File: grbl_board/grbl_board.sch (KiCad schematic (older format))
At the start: 6 parts, among them J1 COOL, J2 12VDC

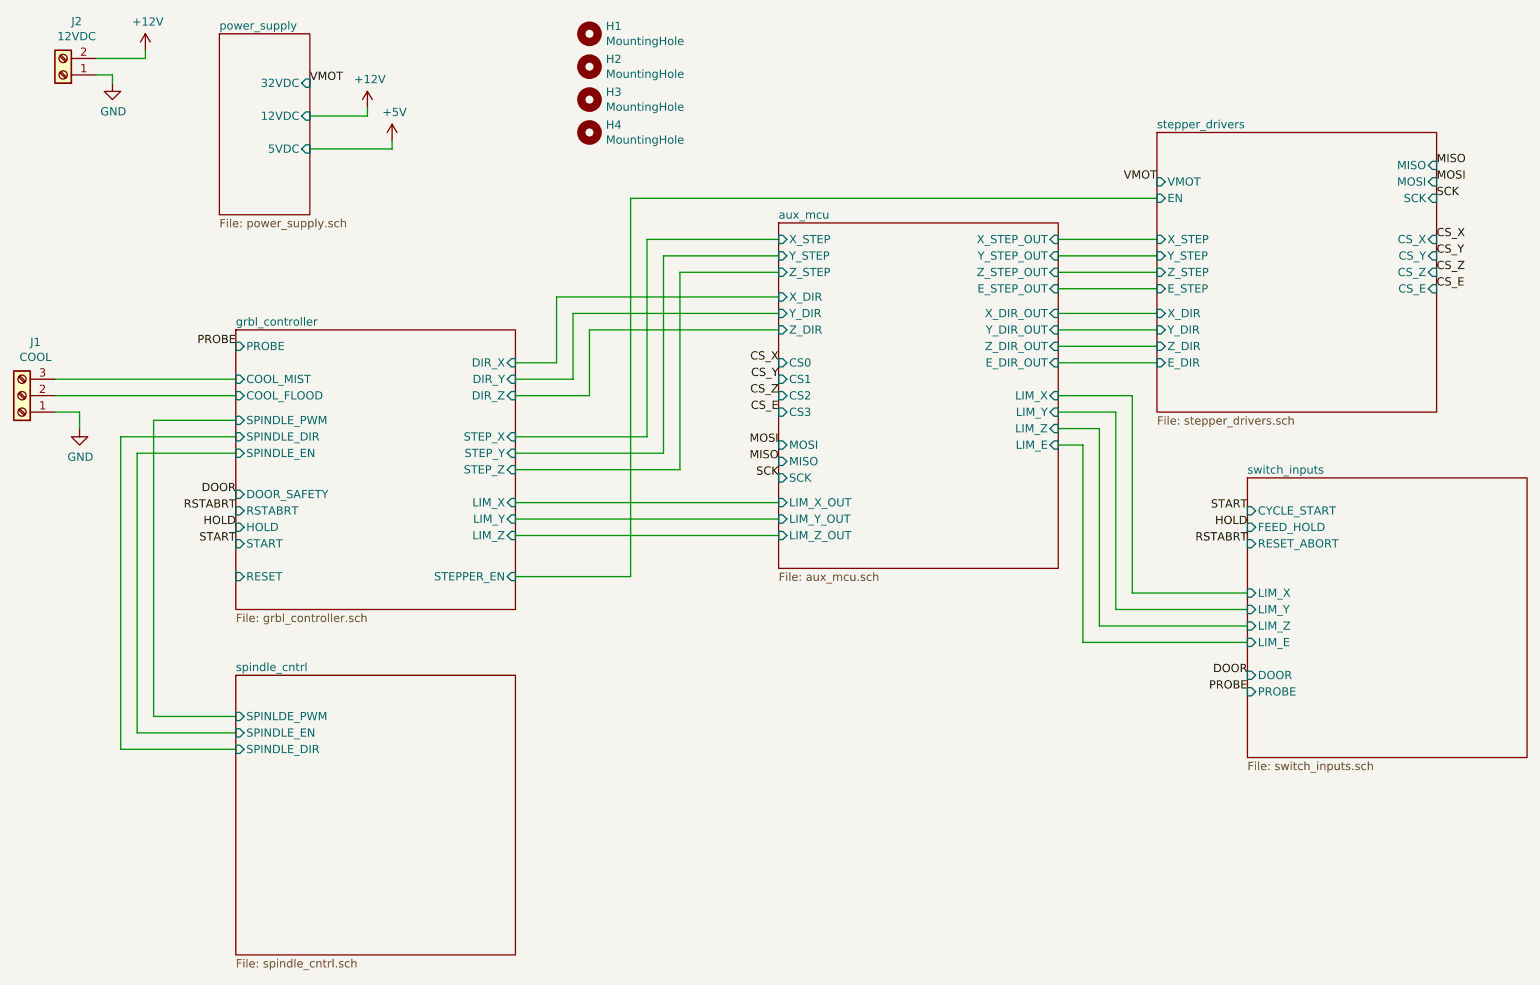
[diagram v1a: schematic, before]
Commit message: updated board with 24V reg
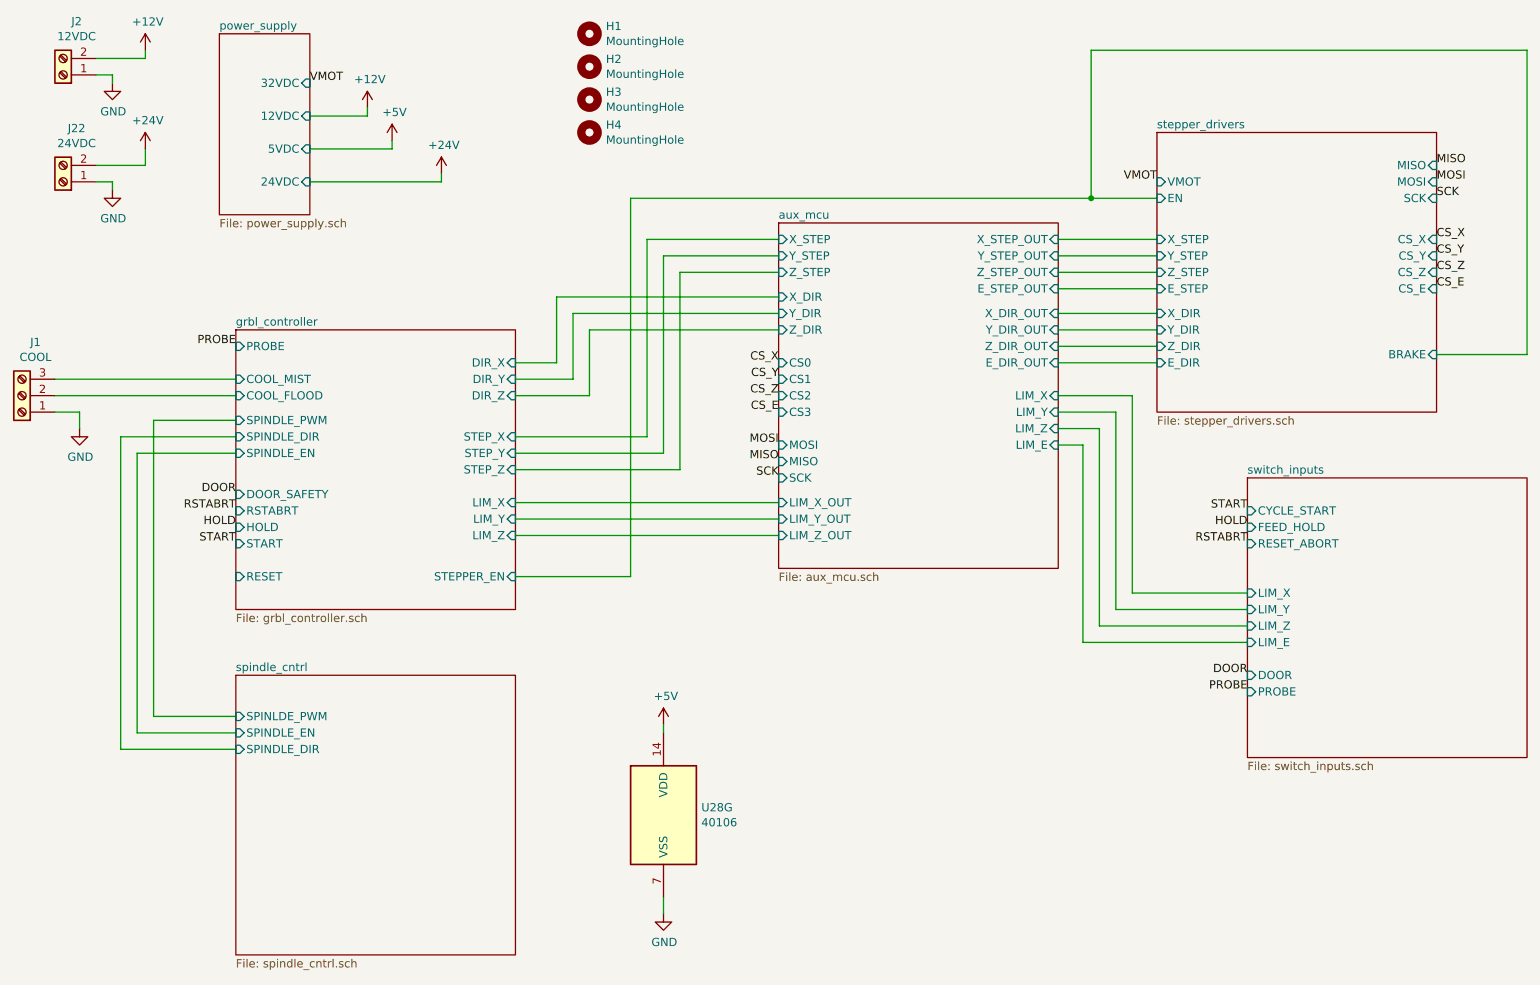
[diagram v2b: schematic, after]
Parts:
- added J22: 24VDC, Connector_Phoenix_MC:PhoenixContact_MC_1,5_2-G-3.81_1x02_P3.81mm_Horizontal, symbol Connector:Screw_Terminal_01x02
- added U28: 40106, Package_SO:TSSOP-14_4.4x5mm_P0.65mm, symbol 4xxx:40106
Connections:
- net +5V: now also U28.14 (VDD)
- net GND: now also J22.1 (Pin_1), U28.7 (VSS)
- new net +24V: J22.2 (Pin_2)
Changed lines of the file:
@@
 F3 "12VDC" I R 2600 1400 50
 F4 "5VDC" I R 2600 1600 50
+F5 "24VDC" I R 2600 1800 50
 $EndSheet
 $Comp
@@
 F17 "E_STEP" I L 7750 2450 50
 F18 "E_DIR" I L 7750 2900 50
+F19 "BRAKE" I R 9450 2850 50
 $EndSheet
 $Comp
@@
 SCK
 Wire Wire Line
-	7750 1900 4550 1900
+	7750 1900 7350 1900
 Wire Wire Line
 	4550 1900 4550 4200
@@
 	1    0    0    -1
 $EndComp
+$Comp
+L power:+24V #PWR06
+U 1 1 61D9341F
+P 3400 1750
+F 0 "#PWR06" H 3400 1600 50  0001 C CNN
+F 1 "+24V" H 3415 1923 50  0000 C CNN
+F 2 "" H 3400 1750 50  0001 C CNN
+F 3 "" H 3400 1750 50  0001 C CNN
+	1    3400 1750
+	1    0    0    -1
+$EndComp
+Wire Wire Line
+	3400 1750 3400 1800
+Wire Wire Line
+	3400 1800 2600 1800
+$Comp
+L Connector:Screw_Terminal_01x02 J22
+U 1 1 62079499
+P 1100 1800
+F 0 "J22" H 1018 1475 50  0000 C CNN
+F 1 "24VDC" H 1018 1566 50  0000 C CNN
+F 2 "Connector_Phoenix_MC:PhoenixContact_MC_1,5_2-G-3.81_1x02_P3.81mm_Horizontal" H 1100 1800 50  0001 C CNN
+F 3 "~" H 1100 1800 50  0001 C CNN
+F 4 "ED2808-ND" H 1100 1800 50  0001 C CNN "Digikey Part No."
+	1    1100 1800
+	-1   0    0    1
+$EndComp
+$Comp
+L power:GND #PWR0111
+U 1 1 6207949F
+P 1400 1850
+F 0 "#PWR0111" H 1400 1600 50  0001 C CNN
+F 1 "GND" H 1405 1677 50  0000 C CNN
+F 2 "" H 1400 1850 50  0001 C CNN
+F 3 "" H 1400 1850 50  0001 C CNN
+	1    1400 1850
+	1    0    0    -1
+$EndComp
+Wire Wire Line
+	1400 1850 1400 1800
+Wire Wire Line
+	1400 1800 1300 1800
+Wire Wire Line
+	1600 1700 1300 1700
+$Comp
+L power:+24V #PWR0112
+U 1 1 6207D4E2
+P 1600 1600
+F 0 "#PWR0112" H 1600 1450 50  0001 C CNN
+F 1 "+24V" H 1615 1773 50  0000 C CNN
+F 2 "" H 1600 1600 50  0001 C CNN
+F 3 "" H 1600 1600 50  0001 C CNN
+	1    1600 1600
+	1    0    0    -1
+$EndComp
+Wire Wire Line
+	1600 1600 1600 1700
+Wire Wire Line
+	4750 5150 4750 5100
+Wire Wire Line
+	4750 6150 4750 6250
+$Comp
+L power:GND #PWR?
+U 1 1 6212F764
+P 4750 6250
+AR Path="/61764E0B/6212F764" Ref="#PWR?"  Part="1"
+AR Path="/6212F764" Ref="#PWR094"  Part="1"
+F 0 "#PWR094" H 4750 6000 50  0001 C CNN
+F 1 "GND" H 4755 6077 50  0000 C CNN
+F 2 "" H 4750 6250 50  0001 C CNN
+F 3 "" H 4750 6250 50  0001 C CNN
+	1    4750 6250
+	1    0    0    -1
+$EndComp
+$Comp
+L power:+5V #PWR?
+U 1 1 6212F76A
+P 4750 5100
+AR Path="/61764E0B/6212F76A" Ref="#PWR?"  Part="1"
+AR Path="/6212F76A" Ref="#PWR036"  Part="1"
+F 0 "#PWR036" H 4750 4950 50  0001 C CNN
+F 1 "+5V" H 4765 5273 50  0000 C CNN
+F 2 "" H 4750 5100 50  0001 C CNN
+F 3 "" H 4750 5100 50  0001 C CNN
+	1    4750 5100
+	1    0    0    -1
+$EndComp
+$Comp
+L 4xxx:40106 U?
+U 7 1 6212F771
+P 4750 5650
+AR Path="/61764E0B/6212F771" Ref="U?"  Part="7"
+AR Path="/6212F771" Ref="U28"  Part="7"
+F 0 "U28" H 4980 5696 50  0000 L CNN
+F 1 "40106" H 4980 5605 50  0000 L CNN
+F 2 "Package_SO:TSSOP-14_4.4x5mm_P0.65mm" H 4750 5650 50  0001 C CNN
+F 3 "https://assets.nexperia.com/documents/data-sheet/HEF40106B.pdf" H 4750 5650 50  0001 C CNN
+F 4 "HEF40106BTT,112-ND" H 4750 5650 50  0001 C CNN "Digikey Part No."
+	7    4750 5650
+	1    0    0    -1
+$EndComp
+Wire Wire Line
+	7350 1900 7350 1000
+Wire Wire Line
+	7350 1000 10000 1000
+Wire Wire Line
+	10000 1000 10000 2850
+Wire Wire Line
+	10000 2850 9450 2850
+Connection ~ 7350 1900
+Wire Wire Line
+	7350 1900 4550 1900
 $EndSCHEMATC
